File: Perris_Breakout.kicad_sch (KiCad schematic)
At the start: 17 parts, among them J1 PERRI_1, J10 SCL_Microcontroller, J11 Conn_01x01_Male, J12 SCL_Microcontroller, J13 Conn_01x01_Male, J14 SCL_Microcontroller, J2 PERRI_2, J3 PERRI_3, J4 PERRI_4, J5 PERRI_5, J6 PERRI_6, J7 PERRI_7, J8 PERRI_8, J9 Conn_01x01_Male

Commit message: Finished Perri I2C Breakout Board
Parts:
- J10: value SCL_Microcontroller -> SCL
- J11: value Conn_01x01_Male -> GND
- J12: value SCL_Microcontroller -> GND
- J13: value Conn_01x01_Male -> SDA
- J14: value SCL_Microcontroller -> SDA
- J9: value Conn_01x01_Male -> SCL
- TP1: value SCL_Test -> SCL
- TP2: value SCL_Test -> GND
- TP3: value SCL_Test -> SDA
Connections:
- net GND: now also J11.1 (Pin_1), J12.1 (Pin_1), TP2.1; no longer J13.1 (Pin_1), J14.1 (Pin_1), TP3.1
- net SDA: now also J13.1 (Pin_1), J14.1 (Pin_1), TP3.1; no longer J11.1 (Pin_1), J12.1 (Pin_1), TP2.1
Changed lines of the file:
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@@
     (effects (font (size 1.27 1.27)) (justify left bottom))
   )
-  (label "SDA" (at 199.39 110.49 90)
+  (label "GND" (at 199.39 110.49 90)
     (effects (font (size 1.27 1.27)) (justify left bottom))
   )
@@
     (effects (font (size 1.27 1.27)) (justify left bottom))
   )
-  (label "GND" (at 199.39 124.46 90)
+  (label "SDA" (at 199.39 124.46 90)
     (effects (font (size 1.27 1.27)) (justify left bottom))
   )
@@
   (symbol (lib_id "Connector:Conn_01x01_Male") (at 186.69 82.55 270) (unit 1)
     (in_bom yes) (on_board yes)
-    (property "Reference" "J9" (id 0) (at 187.96 81.9149 90)
-      (effects (font (size 1.27 1.27)) (justify left))
-    )
-    (property "Value" "Conn_01x01_Male" (id 1) (at 166.37 86.36 90)
+    (property "Reference" "J9" (id 0) (at 180.34 81.28 90)
+      (effects (font (size 1.27 1.27)) (justify left))
+    )
+    (property "Value" "SCL" (id 1) (at 180.34 83.82 90)
       (effects (font (size 1.27 1.27)) (justify left))
     )
@@
       (effects (font (size 1.27 1.27)) (justify left))
     )
-    (property "Value" "SCL_Test" (id 1) (at 200.66 88.8999 0)
+    (property "Value" "SCL" (id 1) (at 200.66 88.8999 0)
       (effects (font (size 1.27 1.27)) (justify left))
     )
@@
   (symbol (lib_id "Connector:Conn_01x01_Male") (at 186.69 97.79 270) (unit 1)
     (in_bom yes) (on_board yes)
-    (property "Reference" "J11" (id 0) (at 187.96 97.1549 90)
-      (effects (font (size 1.27 1.27)) (justify left))
-    )
-    (property "Value" "Conn_01x01_Male" (id 1) (at 166.37 101.6 90)
+    (property "Reference" "J11" (id 0) (at 181.61 96.52 90)
+      (effects (font (size 1.27 1.27)) (justify left))
+    )
+    (property "Value" "GND" (id 1) (at 180.34 99.06 90)
       (effects (font (size 1.27 1.27)) (justify left))
     )
@@
       (effects (font (size 1.27 1.27)) (justify left))
     )
-    (property "Value" "SCL_Microcontroller" (id 1) (at 220.98 99.6949 90)
+    (property "Value" "GND" (id 1) (at 220.98 99.6949 90)
       (effects (font (size 1.27 1.27)) (justify left))
     )
@@
       (effects (font (size 1.27 1.27)) (justify left))
     )
-    (property "Value" "SCL_Test" (id 1) (at 200.66 104.1399 0)
+    (property "Value" "GND" (id 1) (at 200.66 104.1399 0)
       (effects (font (size 1.27 1.27)) (justify left))
     )
@@
       (effects (font (size 1.27 1.27)) (justify left))
     )
-    (property "Value" "SCL_Microcontroller" (id 1) (at 220.98 113.6649 90)
+    (property "Value" "SDA" (id 1) (at 220.98 113.6649 90)
       (effects (font (size 1.27 1.27)) (justify left))
     )
@@
       (effects (font (size 1.27 1.27)) (justify left))
     )
-    (property "Value" "SCL_Test" (id 1) (at 200.66 118.1099 0)
+    (property "Value" "SDA" (id 1) (at 200.66 118.1099 0)
       (effects (font (size 1.27 1.27)) (justify left))
     )
@@
       (effects (font (size 1.27 1.27)) (justify left))
     )
-    (property "Value" "Conn_01x01_Male" (id 1) (at 166.37 115.57 90)
+    (property "Value" "SDA" (id 1) (at 187.96 114.3 90)
       (effects (font (size 1.27 1.27)) (justify left))
     )
@@
       (effects (font (size 1.27 1.27)) (justify left))
     )
-    (property "Value" "SCL_Microcontroller" (id 1) (at 220.98 84.4549 90)
+    (property "Value" "SCL" (id 1) (at 220.98 84.4549 90)
       (effects (font (size 1.27 1.27)) (justify left))
     )
@@
     )
     (path "/01f3def0-727f-4ff4-91f6-12fdb6a71365"
-      (reference "J9") (unit 1) (value "Conn_01x01_Male") (footprint "Connector_PinHeader_2.54mm:PinHeader_1x01_P2.54mm_Vertical")
+      (reference "J9") (unit 1) (value "SCL") (footprint "Connector_PinHeader_2.54mm:PinHeader_1x01_P2.54mm_Vertical")
     )
     (path "/f99fda44-c812-4a3a-9c29-0f7fbd064e64"
-      (reference "J10") (unit 1) (value "SCL_Microcontroller") (footprint "Connector_PinHeader_2.54mm:PinHeader_1x01_P2.54mm_Vertical")
+      (reference "J10") (unit 1) (value "SCL") (footprint "Connector_PinHeader_2.54mm:PinHeader_1x01_P2.54mm_Vertical")
     )
     (path "/24a12225-cf2f-4e3e-b597-f90f877d89bf"
-      (reference "J11") (unit 1) (value "Conn_01x01_Male") (footprint "Connector_PinHeader_2.54mm:PinHeader_1x01_P2.54mm_Vertical")
+      (reference "J11") (unit 1) (value "GND") (footprint "Connector_PinHeader_2.54mm:PinHeader_1x01_P2.54mm_Vertical")
     )
     (path "/2be63412-6a95-4b9a-af83-beb545a6ee74"
-      (reference "J12") (unit 1) (value "SCL_Microcontroller") (footprint "Connector_PinHeader_2.54mm:PinHeader_1x01_P2.54mm_Vertical")
+      (reference "J12") (unit 1) (value "GND") (footprint "Connector_PinHeader_2.54mm:PinHeader_1x01_P2.54mm_Vertical")
     )
     (path "/af41b548-bfca-440d-9bee-d6335779e8e5"
-      (reference "J13") (unit 1) (value "Conn_01x01_Male") (footprint "Connector_PinHeader_2.54mm:PinHeader_1x01_P2.54mm_Vertical")
+      (reference "J13") (unit 1) (value "SDA") (footprint "Connector_PinHeader_2.54mm:PinHeader_1x01_P2.54mm_Vertical")
     )
     (path "/3c5c2ab2-2def-494c-9a03-87ee7c16e836"
-      (reference "J14") (unit 1) (value "SCL_Microcontroller") (footprint "Connector_PinHeader_2.54mm:PinHeader_1x01_P2.54mm_Vertical")
+      (reference "J14") (unit 1) (value "SDA") (footprint "Connector_PinHeader_2.54mm:PinHeader_1x01_P2.54mm_Vertical")
     )
     (path "/1a38f442-37f1-4c0d-b639-48acf70bf662"
-      (reference "TP1") (unit 1) (value "SCL_Test") (footprint "TestPoint:TestPoint_Pad_2.5x2.5mm")
+      (reference "TP1") (unit 1) (value "SCL") (footprint "TestPoint:TestPoint_Pad_2.5x2.5mm")
     )
     (path "/3a03a9f2-3b31-49df-b740-9fe8bd6dc7ac"
-      (reference "TP2") (unit 1) (value "SCL_Test") (footprint "TestPoint:TestPoint_Pad_2.5x2.5mm")
+      (reference "TP2") (unit 1) (value "GND") (footprint "TestPoint:TestPoint_Pad_2.5x2.5mm")
     )
     (path "/4f164f8e-bc3b-4e49-bbb8-c1d623c879a3"
-      (reference "TP3") (unit 1) (value "SCL_Test") (footprint "TestPoint:TestPoint_Pad_2.5x2.5mm")
-    )
-  )
+      (reference "TP3") (unit 1) (value "SDA") (footprint "TestPoint:TestPoint_Pad_2.5x2.5mm")
+    )
+  )

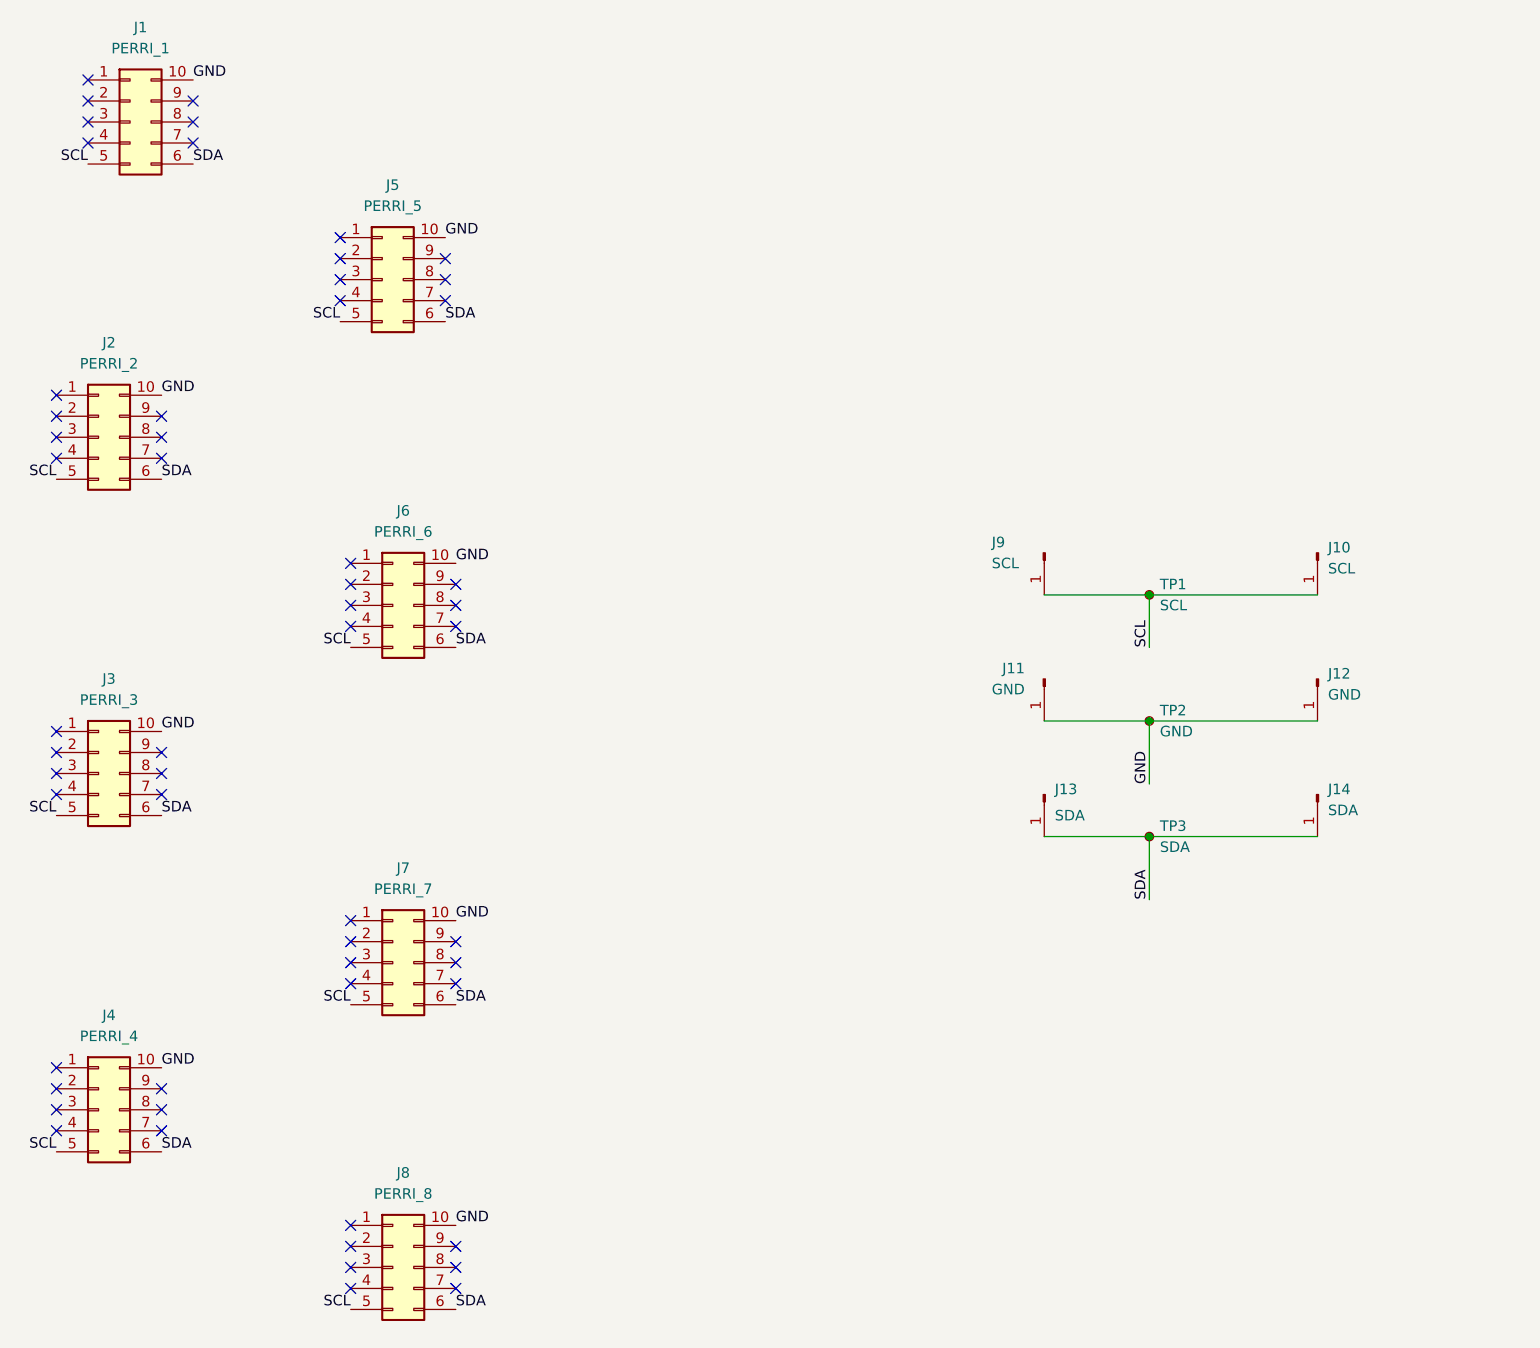
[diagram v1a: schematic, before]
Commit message: Updated PCB with ground plane surroudning connectors.
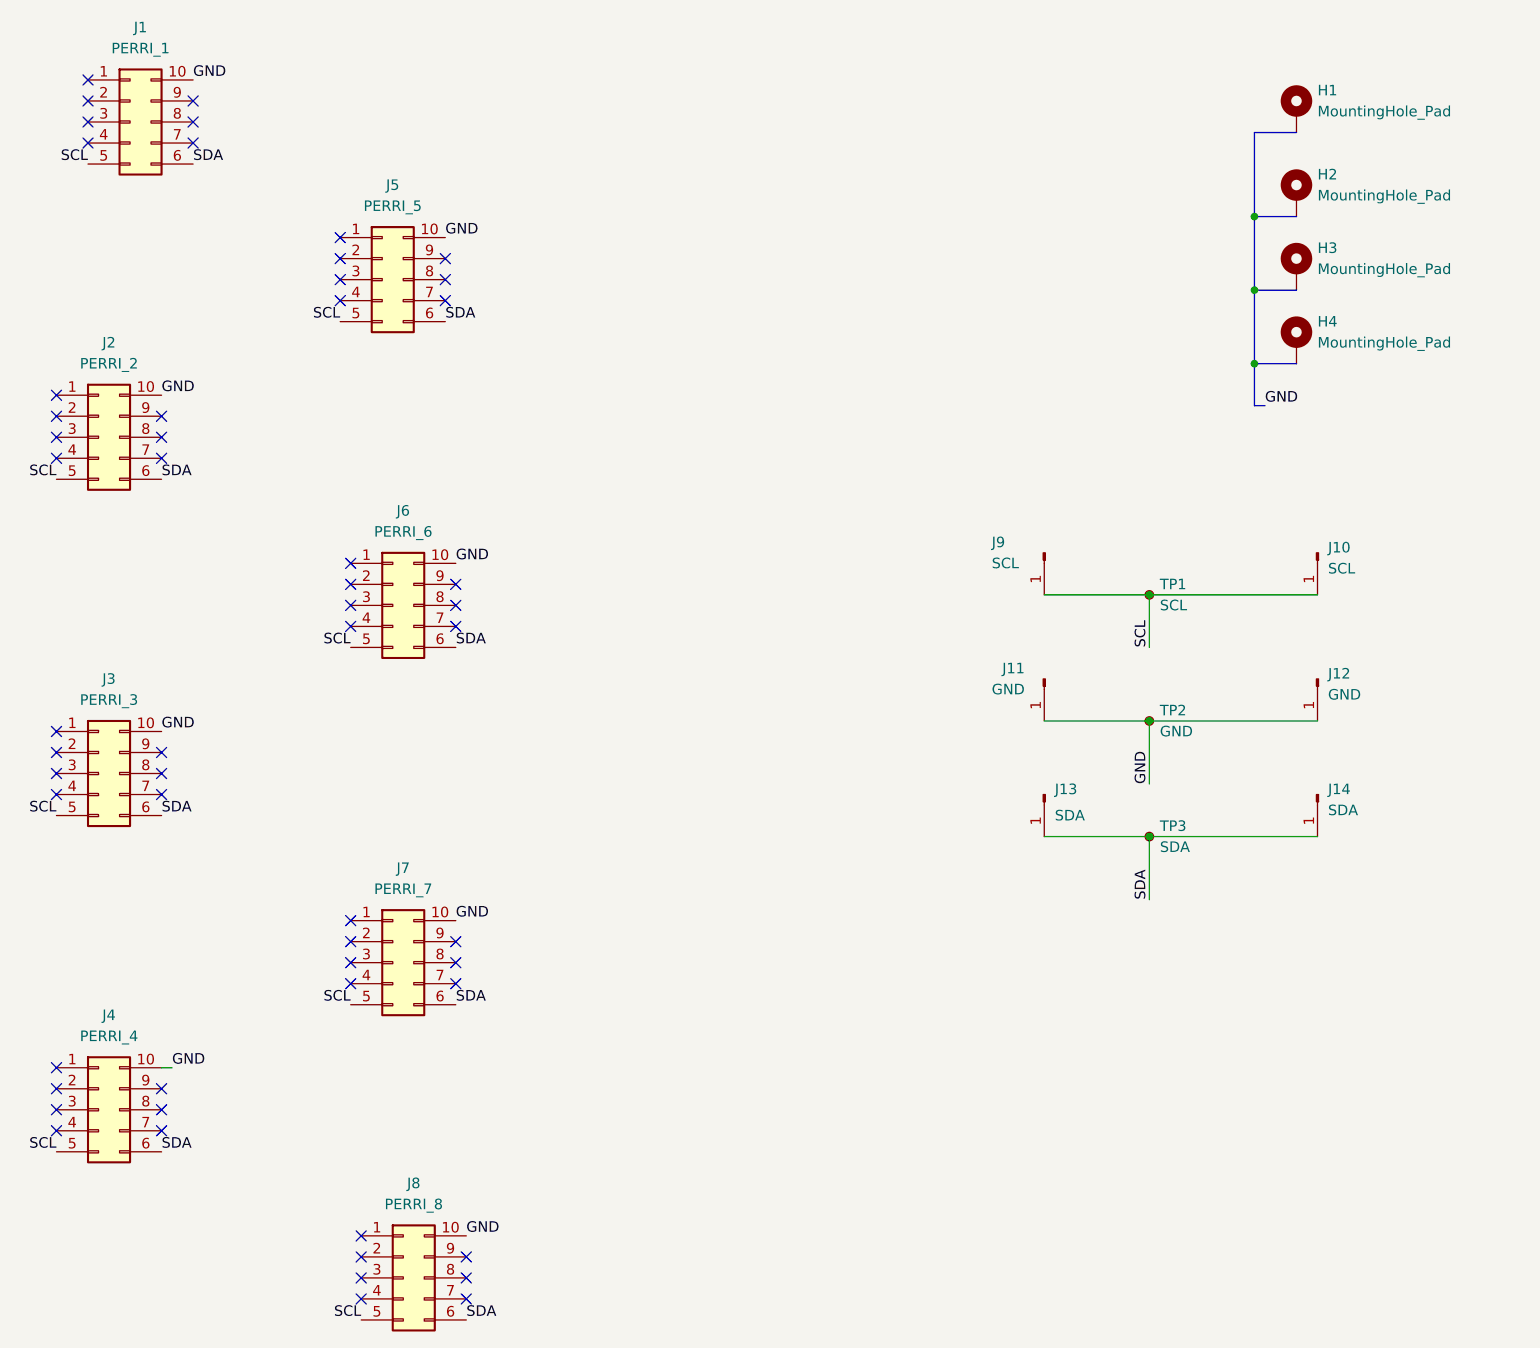
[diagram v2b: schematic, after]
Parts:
- added H1, H2, H3, H4: MountingHole_Pad, MountingHole:MountingHole_3.2mm_M3_ISO7380_Pad, symbol Mechanical:MountingHole_Pad
- TP1, TP2, TP3: footprint TestPoint:TestPoint_Pad_2.5x2.5mm -> Connector_PinHeader_2.54mm:PinHeader_1x01_P2.54mm_Vertical
